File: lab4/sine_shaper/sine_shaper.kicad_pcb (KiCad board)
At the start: 2 copper layers, 41 x 32 mm, 30 parts, among them J1 Conn_01x02_Male, J2 Screw_Terminal_01x03, J3 Conn_01x02_Male, Q1 MMBT3904, Q2 MMBT3904, Q3 MMBT3904, U1 LM358

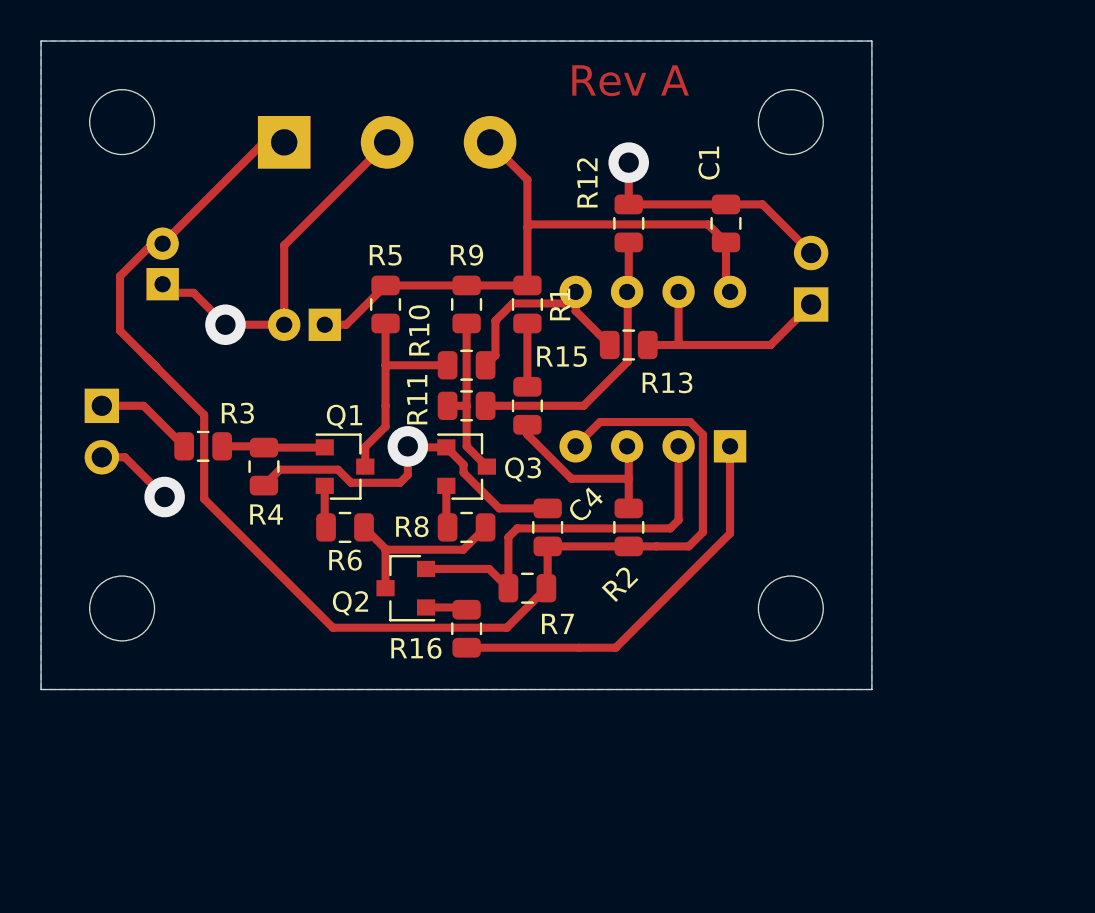
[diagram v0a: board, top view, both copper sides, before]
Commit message: Finish function generator
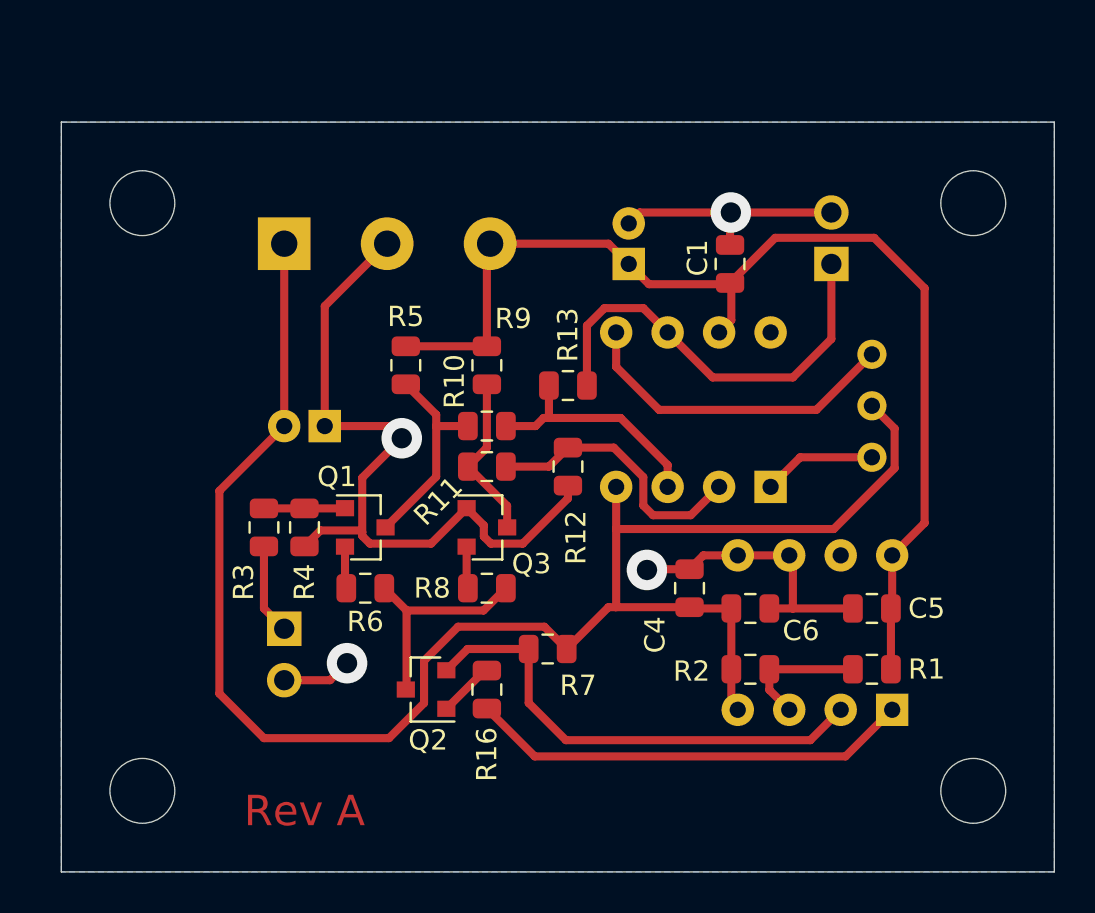
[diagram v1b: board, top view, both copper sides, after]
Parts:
- removed R15: 0R, Resistor_SMD:R_0805_2012Metric
- added C5: 0.1uF, Capacitor_SMD:C_0805_2012Metric, F.Cu at (148.0, 100.0)
- added C6: 0.1uF, Capacitor_SMD:C_0805_2012Metric, F.Cu at (142.0, 100.0)
- added RV1: 10k, Potentiometer_THT:Potentiometer_Bourns_3296W_Vertical, B.Cu at (148.0, 87.5)
- added U2: LF356, Package_DIP:DIP-8_W7.62mm, B.Cu at (143.0, 94.0)
- R10, R11: value 12M -> 1.2M
- R12, R13: value 1M -> 100k
- moved R1 24.8 mm to (148.0, 103.0), turned to 180 degrees
- moved C2 15.3 mm to (136.0, 83.0), turned to 90 degrees
- moved U1 15.3 mm to (149.0, 105.0)
- moved J3 14.2 mm to (119.0, 101.0)
- moved H3 12.7 mm to (153.0, 109.0)
- moved R12 12.4 mm to (133.0, 93.0), turned to 90 degrees
- moved C3 10.6 mm to (121.0, 91.0), turned to 180 degrees
- moved H2 9.85 mm to (153.0, 80.0)
- moved R2 9.22 mm to (142.0, 103.0), turned to 180 degrees
- moved H4 9.06 mm to (112.0, 109.0)
- moved C4 7.62 mm to (139.0, 99.0)
- moved Q2 5.10 mm to (126.0, 104.0)
- moved J2 5.00 mm to (119.0, 82.0)
- moved R3 5.00 mm to (118.0, 96.0), turned to 270 degrees
- moved H1 4.12 mm to (112.0, 80.0)
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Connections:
- R1 pad 2: Net-(R1-Pad2) -> /CURR_SET
- U1 pad 5: Net-(R10-Pad1) -> GND
- U1 pad 6: Net-(R11-Pad1) -> GND
- U1 pad 7: /SINE_OUT -> (no net)
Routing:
- net +12V: track 31.4 -> 55.5 mm
- net -12V: track 67.5 -> 84.1 mm
- net Net-(RV1-Pad1): track 0.00 -> 16.3 mm
- net GND: track 51.0 -> 66.2 mm
- net /SINE_OUT: track 11.6 -> 21.3 mm
- net Net-(RV1-Pad3): track 0.00 -> 5.60 mm
- net Net-(Q2-Pad2): track 19.4 -> 23.9 mm
- net Net-(R1-Pad2): track 3.12 -> 0.00 mm
- net /CURR_SET: track 9.48 -> 6.53 mm
- net Net-(R16-Pad2): track 19.6 -> 21.9 mm
- net Net-(Q2-Pad3): track 8.83 -> 10.8 mm
- net Net-(R10-Pad1): track 10.3 -> 11.8 mm
- net /TRIANGLE_DIV: track 5.09 -> 4.01 mm
- net Net-(Q2-Pad1): track 2.05 -> 2.78 mm
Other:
- board size 41 x 32 mm -> 49 x 37 mm
- board text added: "SINE OUT"
- board text added: "TRIANGLE IN"
- board text removed: "SINE_OUT"
- board text removed: "TRIANGLE_IN"
